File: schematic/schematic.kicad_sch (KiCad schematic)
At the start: 22 parts, among them J1 Conn_01x19, J2 Conn_01x19, J3 映像入力, J4 映像出力, J5 PCM5102A DACモジュール, J6 GNSSモジュール, J7 MicroSDカードモジュール, J8 2004 LCD, P1 外部給電コネクタ, SW1 電源選択スイッチ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

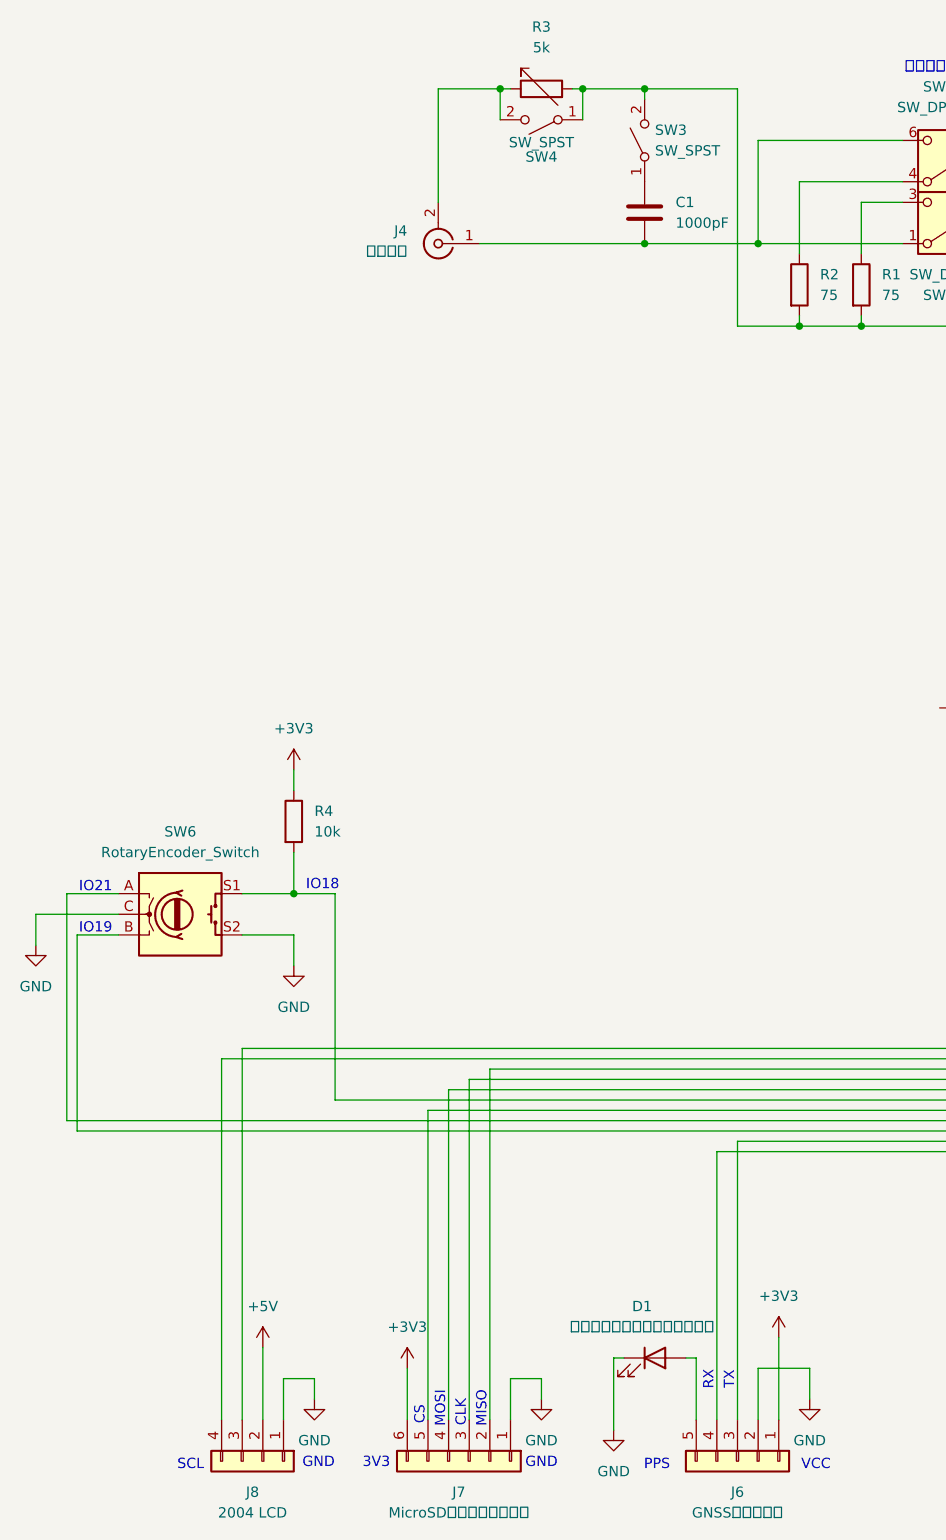
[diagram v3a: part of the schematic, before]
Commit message: Added microphone and audio output
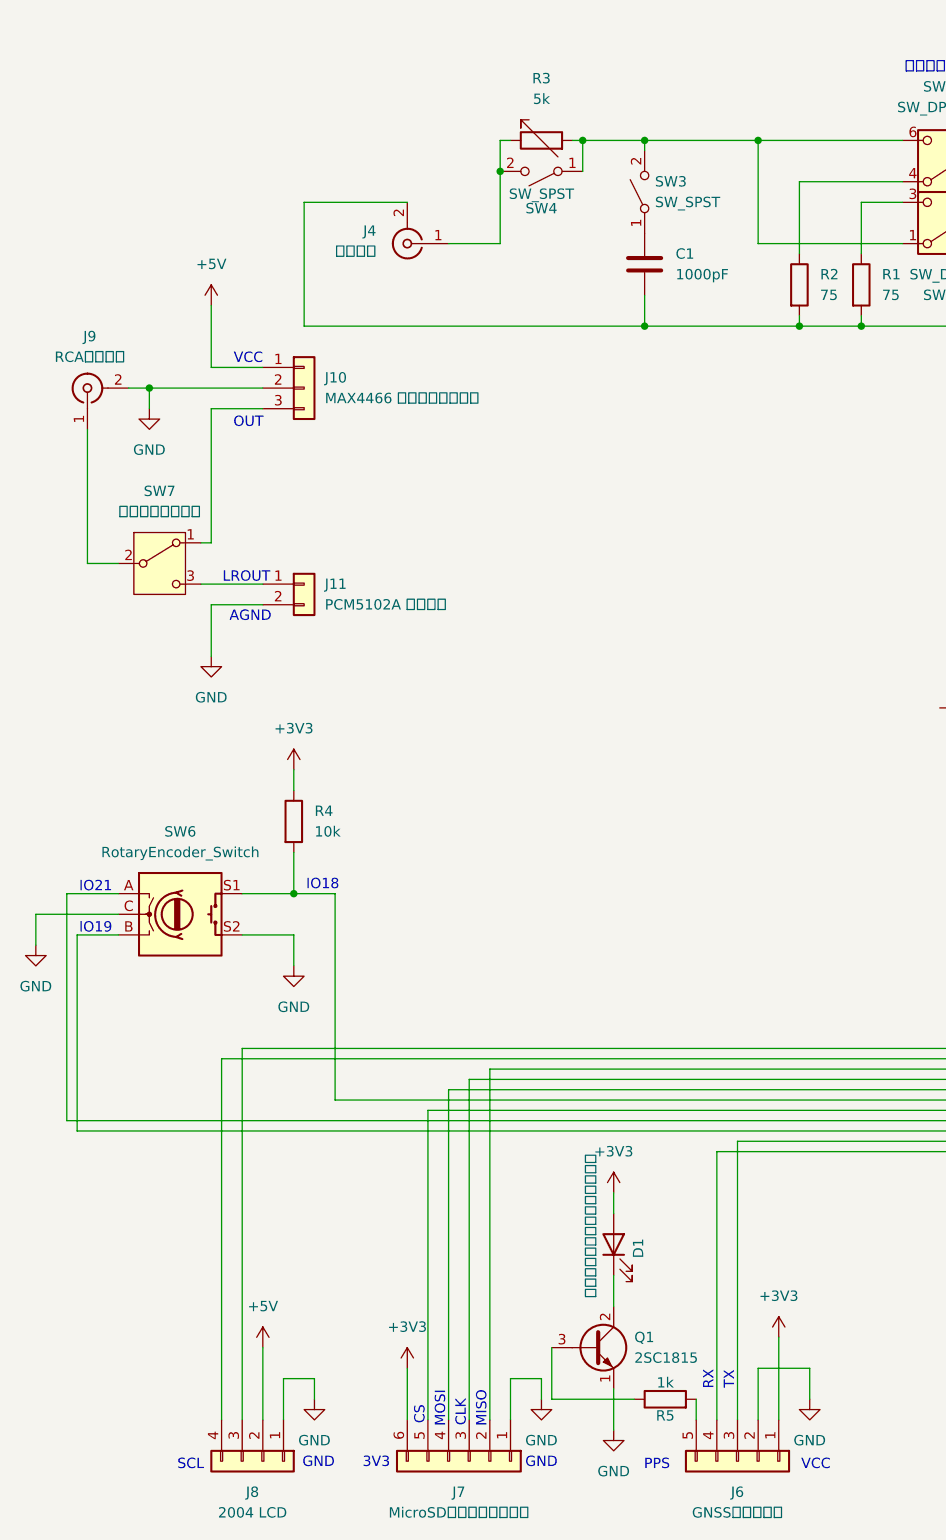
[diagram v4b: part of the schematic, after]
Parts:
- added J10: MAX4466 マイクモジュール, symbol Connector_Generic:Conn_01x03
- added J11: PCM5102A 音声出力, symbol Connector_Generic:Conn_01x02
- added J9: RCA音声出力, symbol Connector:Conn_Coaxial
- added Q1: 2SC1815, Package_TO_SOT_THT:TO-92_Inline, symbol Transistor_BJT:2SC1815
- added R5: 1k, symbol Device:R
- added SW7: 音声選択スイッチ, symbol Switch:SW_SPDT
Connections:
- net +3V3: now also D1.2 (A)
- net +5V: now also J10.1 (Pin_1)
- net GND: now also J10.2 (Pin_2), J11.2 (Pin_2), J9.2 (Ext), Q1.1 (E); no longer D1.1 (K)
- net at J3.2 (Ext), R1.2, R2.2: now also C1.2, J4.2 (Ext); no longer R3.2, SW3.2 (B), SW4.1 (A)
- net at SW2.1 (A), SW2.6 (C): now also R3.2, SW3.2 (B), SW4.1 (A); no longer C1.2, J4.1 (In)
- net at R3.1, SW4.2 (B): now also J4.1 (In); no longer J4.2 (Ext)
- net at J6.5 (Pin_5): now also R5.2; no longer D1.2 (A)
- new net: J10.3 (Pin_3), SW7.1 (A)
- new net: J9.1 (In), SW7.2 (B)
- new net: J11.1 (Pin_1), SW7.3 (C)
- new net: D1.1 (K), Q1.2 (C)
- new net: Q1.3 (B), R5.1
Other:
- note added: "AGND"
- note added: "LROUT"
- note added: "OUT"
- moved on the sheet: C1, D1, J4, R3, SW3, SW4

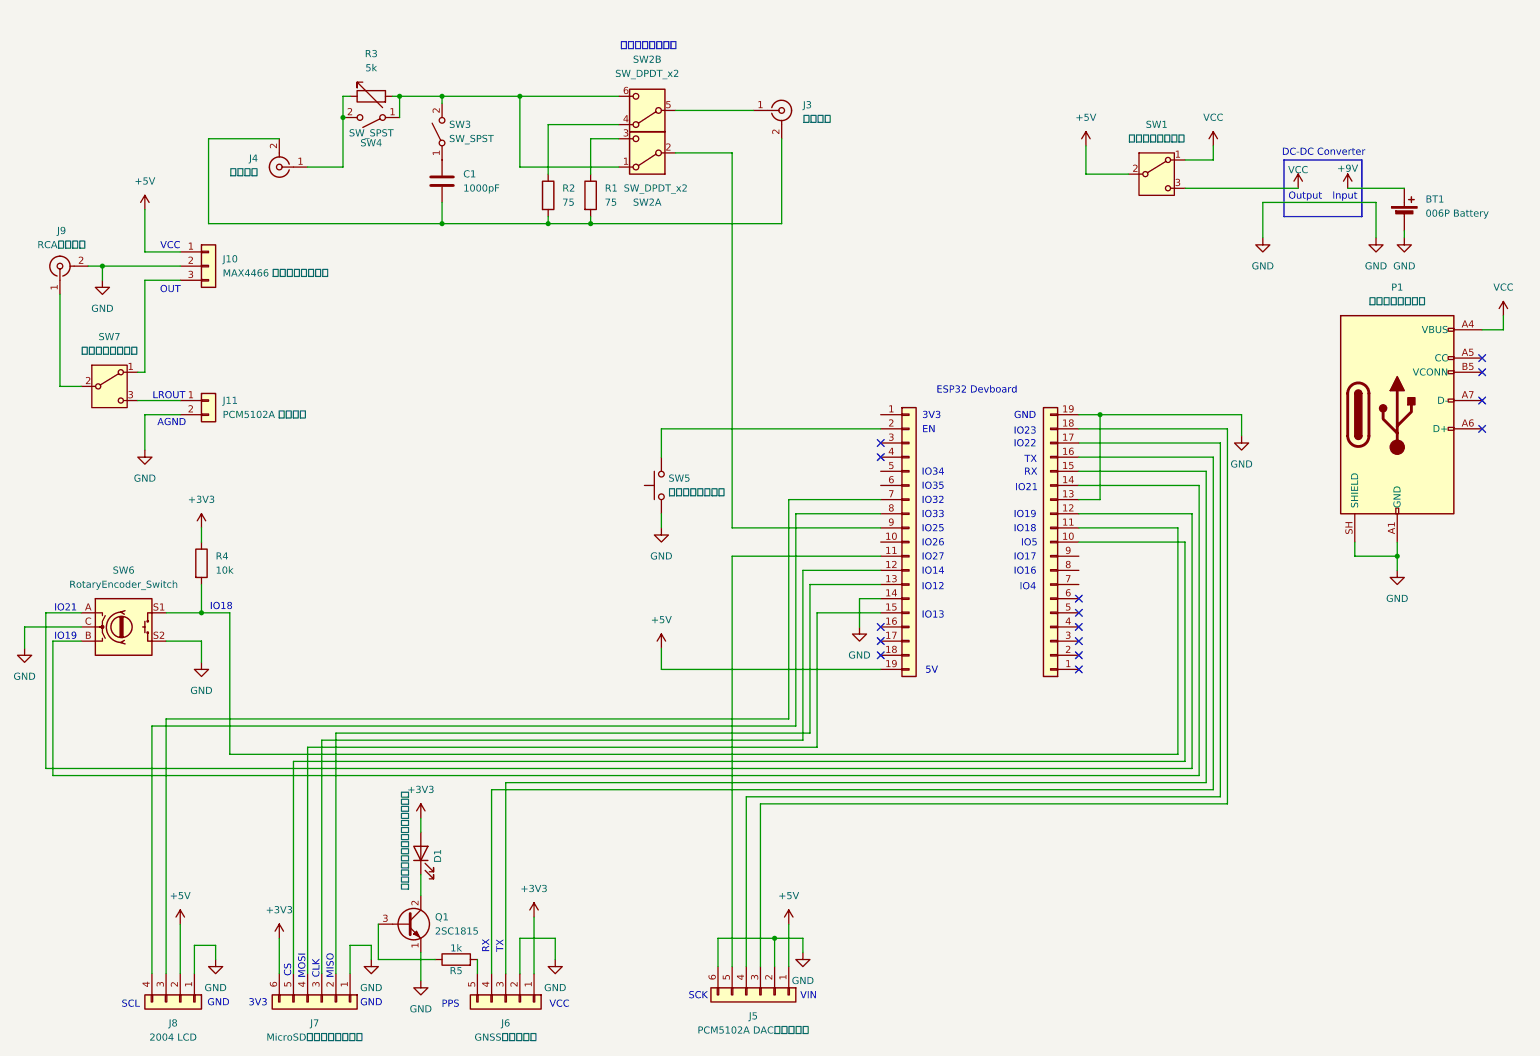
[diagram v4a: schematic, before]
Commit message: Added lid and LED lamps and push buttons.
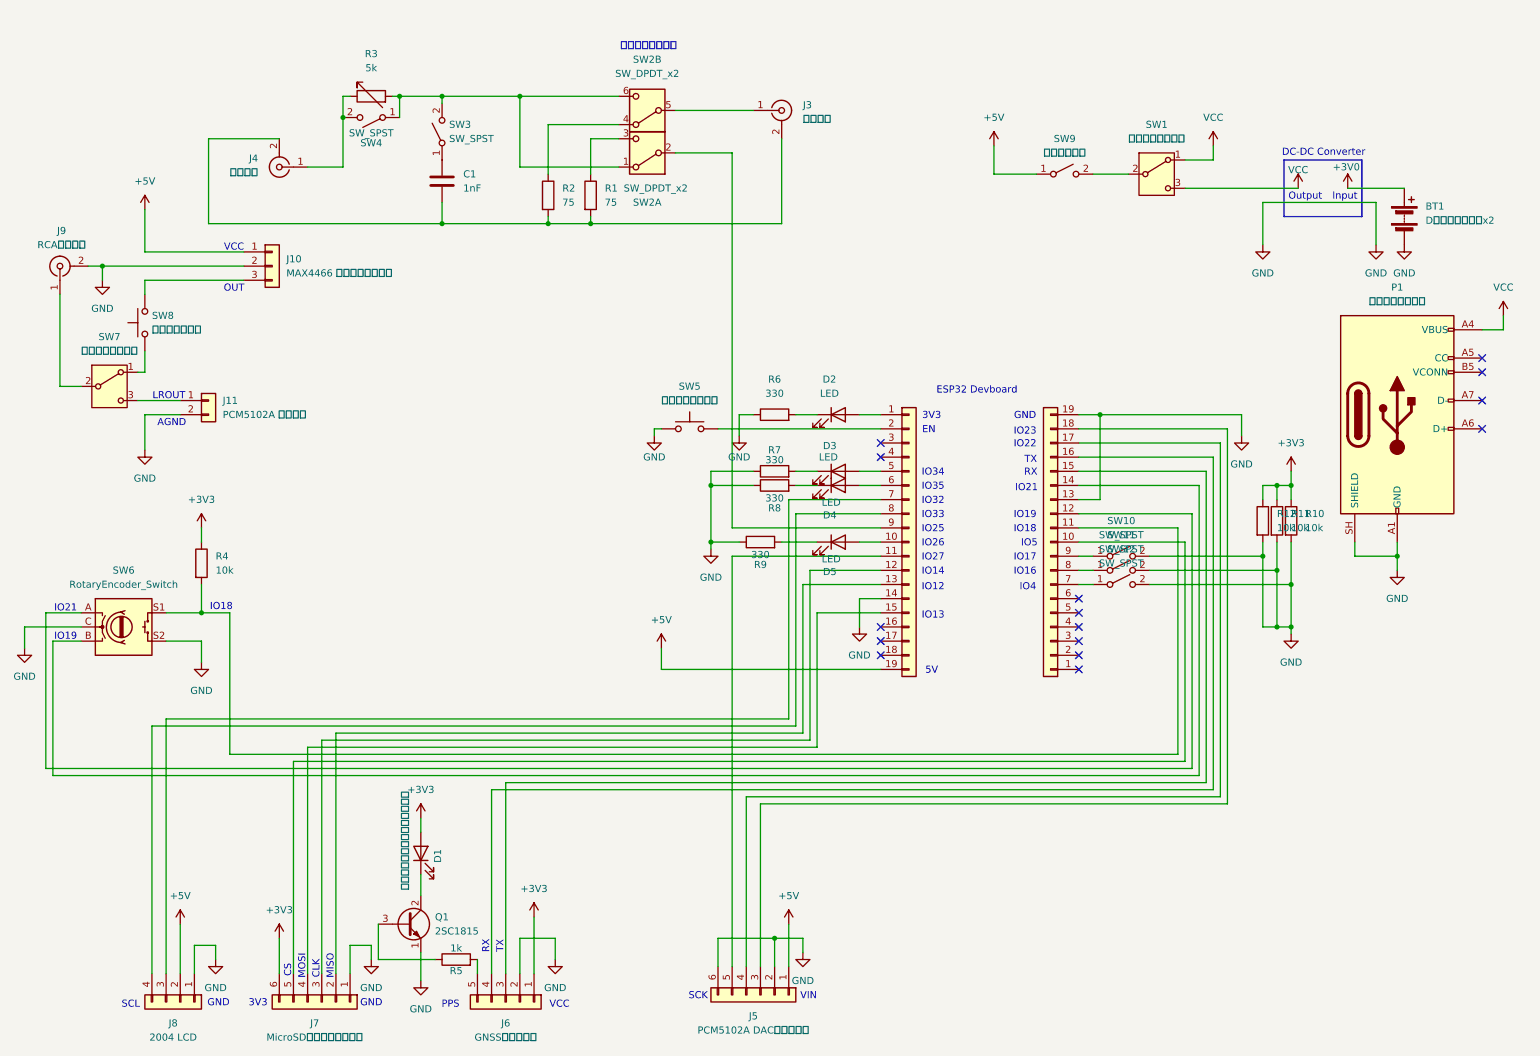
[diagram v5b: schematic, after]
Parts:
- removed BT1: 006P Battery, symbol Device:Battery_Cell
- added BT1: D（単一乾電池）x2, symbol Device:Battery
- added D2, D3, D4, D5: LED, symbol Device:LED
- added R10, R11, R12: 10k, symbol Device:R
- added R6, R7, R8, R9: 330, symbol Device:R
- added SW10, SW11, SW12: SW_SPST, symbol Switch:SW_SPST
- added SW8: オンエアボタン, symbol Switch:SW_Push
- added SW9: 電源スイッチ, symbol Switch:SW_SPST
- C1: value 1000pF -> 1nF
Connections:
- net +3V3: now also R10.1, R11.1, R12.1
- net +5V: now also SW9.1 (A); no longer SW1.2 (B)
- net GND: now also BT1.2 (-), R10.2, R11.2, R12.2, R6.1, R7.1, R8.1, R9.1, SW10.2 (B), SW11.2 (B), SW12.2 (B)
- net at J1.1 (Pin_1): now also D2.2 (A)
- net at J1.10 (Pin_10): now also D5.2 (A)
- net at J1.5 (Pin_5): now also D3.2 (A)
- net at J1.6 (Pin_6): now also D4.2 (A)
- net at SW7.1 (A): now also SW8.1; no longer J10.3 (Pin_3)
- net at J2.7 (Pin_7): now also SW12.1 (A)
- net at J2.8 (Pin_8): now also SW11.1 (A)
- net at J2.9 (Pin_9): now also SW10.1 (A)
- new net: D2.1 (K), R6.2
- new net: D5.1 (K), R9.2
- new net: D4.1 (K), R8.2
- new net: J10.3 (Pin_3), SW8.2
- new net: SW1.2 (B), SW9.2 (B)
- new net: D3.1 (K), R7.2
- new net +3V0: BT1.1 (+)
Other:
- moved on the sheet: J10, SW5
